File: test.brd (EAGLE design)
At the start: 28.9 x 20.9 mm, 14 parts

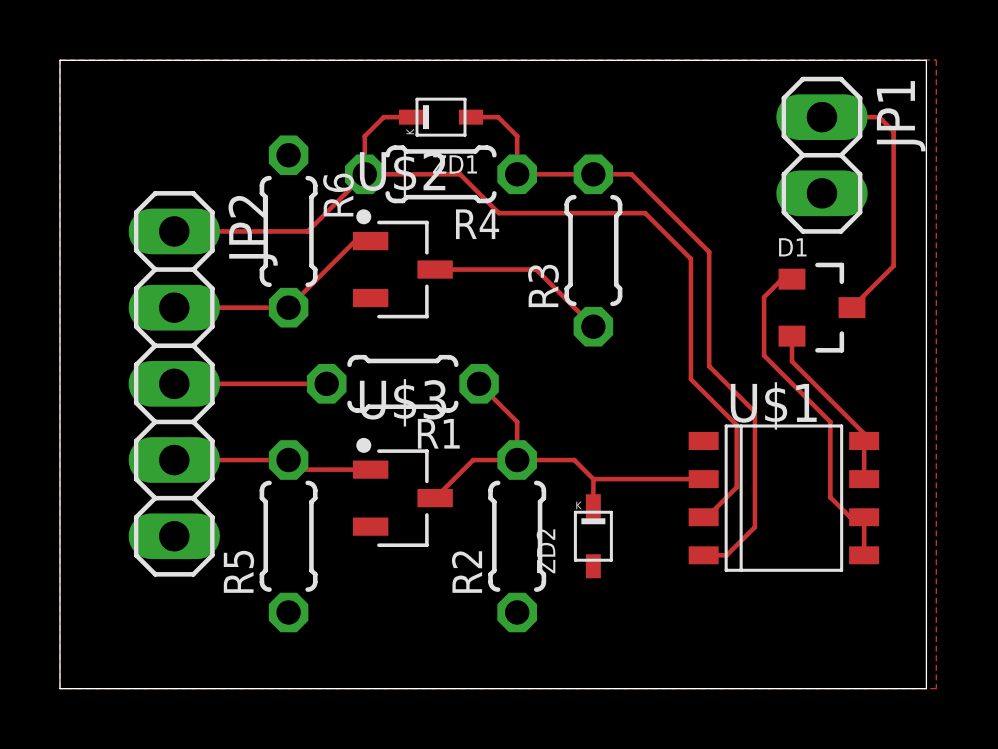
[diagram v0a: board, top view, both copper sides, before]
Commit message: added a NPN for like voltage follower
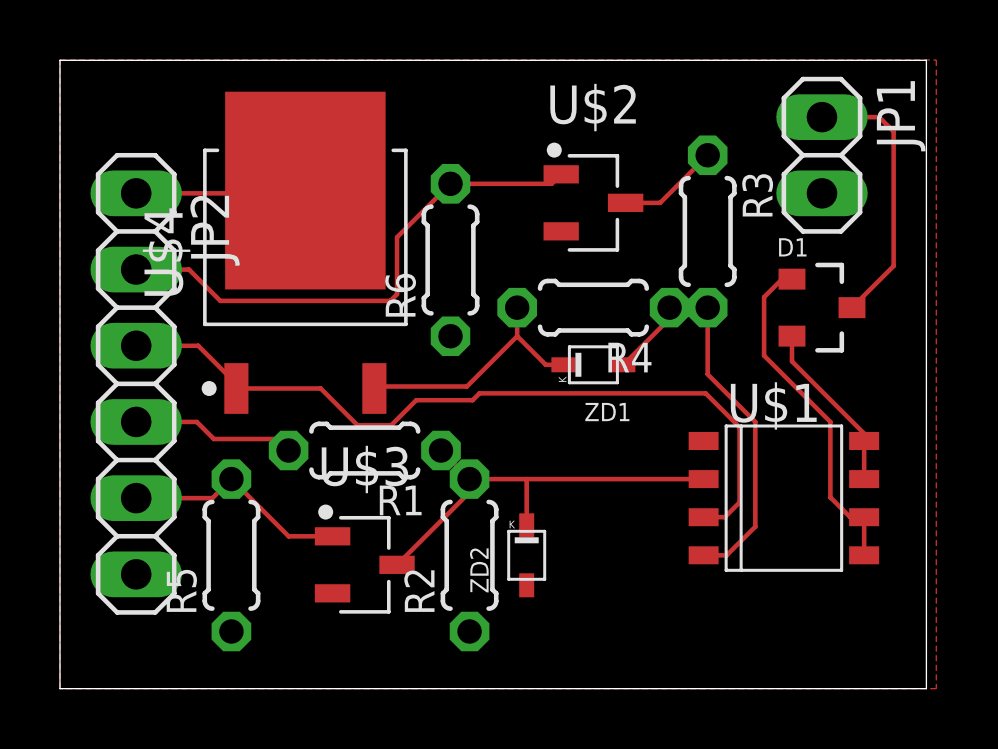
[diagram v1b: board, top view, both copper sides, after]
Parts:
- added U$4: SC3632-Z, Transistor-NPN:TO252(MP-3Z)
- JP2: device pinhead:1X05 -> pinhead:1X06
- moved ZD1 9.69 mm to (17.8, 10.8)
- moved R4 6.75 mm to (17.8, 12.7)
- moved U$2 6.73 mm to (17.8, 16.2)
- moved R6 5.48 mm to (13.0, 14.3), turned to 90 degrees
- moved R3 3.86 mm to (21.6, 15.2), turned to 270 degrees
- moved R1 2.56 mm to (10.2, 7.94)
- moved U$3 2.56 mm to (10.2, 4.13)
- moved ZD2 2.31 mm to (15.6, 4.45)
- moved R5 2.01 mm to (5.71, 4.45)
- moved R2 1.71 mm to (13.7, 4.45)
- moved JP2 1.27 mm to (2.54, 10.2)
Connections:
- new net N$6: R4.2, U$4.2, ZD1.P$1
- new net VDD: JP2.1, U$4.3
- net +12V: now also JP2.4; no longer JP2.3
- net GND: now also JP2.6; no longer JP2.5
- net N$4: now also JP2.5; no longer JP2.4
- net VPP: now also JP2.3, U$4.1; no longer JP2.1, R4.2, ZD1.P$1
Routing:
- net N$5: track 7.47 -> 17.5 mm
- net N$3: track 22.4 -> 13.9 mm
- net N$6: track 0.00 -> 8.37 mm
- net VDD: track 0.00 -> 5.68 mm
- net VPP: track 32.0 -> 26.6 mm
- net N$2: track 6.06 -> 3.39 mm
- net N$4: track 6.68 -> 7.60 mm
- net N$1: track 13.7 -> 14.5 mm

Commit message: rearranged devices
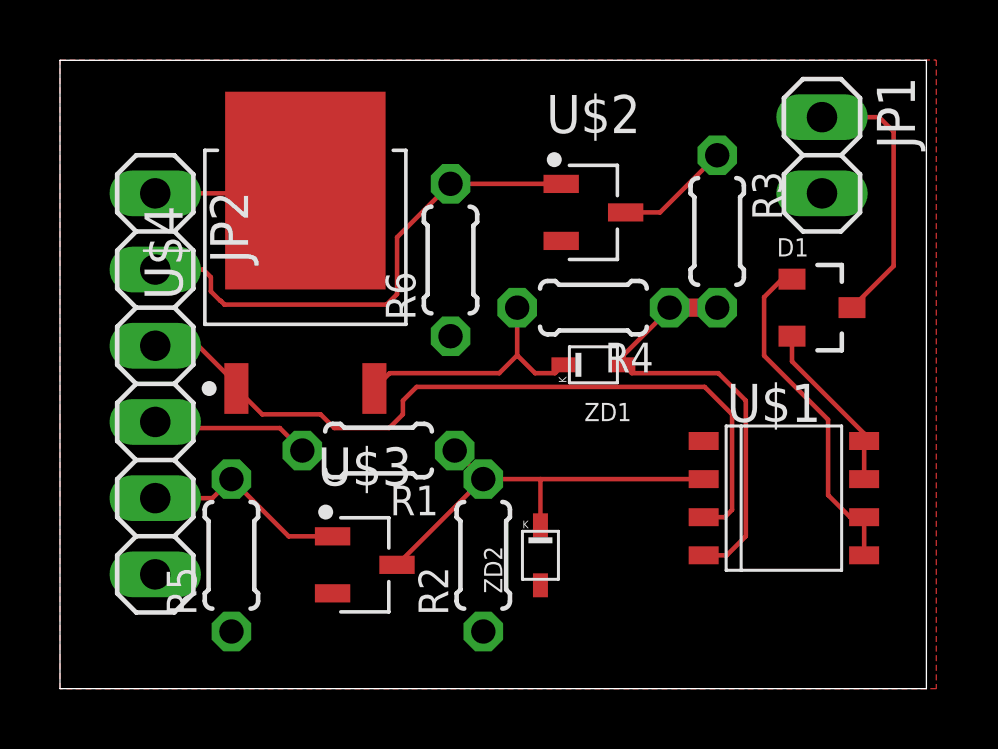
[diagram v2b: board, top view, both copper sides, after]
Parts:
- moved JP2 0.63 mm to (3.17, 10.2)
- moved ZD2 0.46 mm to (16.0, 4.45)
- moved R1 0.46 mm to (10.6, 7.94)
- moved R2 0.46 mm to (14.1, 4.45)
- moved R3 0.32 mm to (21.9, 15.2)
- moved U$2 0.32 mm to (17.8, 15.9)
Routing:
- net N$3: track 13.9 -> 14.9 mm
- net N$5: track 17.5 -> 18.2 mm
- net VPP: track 26.6 -> 25.9 mm
- net VDD: track 5.68 -> 5.04 mm
- net N$4: track 7.60 -> 6.96 mm

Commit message: replace the transistor with FET which compose a source follower.*
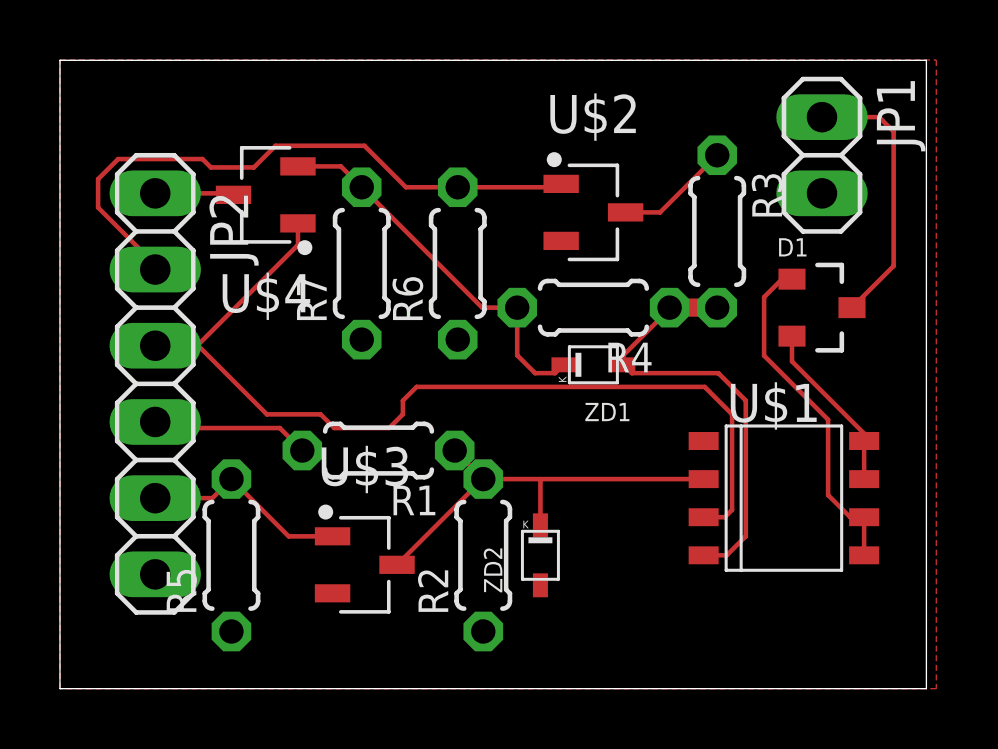
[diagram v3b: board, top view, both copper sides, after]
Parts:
- added R7: 105, rcl:0204/5
- U$4: value SC3632-Z -> 2SK3072-TB-E; device Transistor-NPN:TO252(MP-3Z) -> Transistor-FET:SOT95P250X120-3
- moved U$4 2.34 mm to (6.86, 16.5), turned to 180 degrees
- moved R6 0.27 mm to (13.3, 14.2)
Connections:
- net GND: now also R7.1
- net N$6: now also R7.2
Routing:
- net VPP: track 25.9 -> 31.3 mm
- net N$6: track 8.71 -> 12.7 mm
- net VDD: track 5.04 -> 2.63 mm
- net N$5: track 18.2 -> 20.5 mm
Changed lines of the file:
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@@
 <attribute name="VALUE" x="8.0264" y="2.3114" size="0.9906" layer="27" ratio="10" rot="R90"/>
 </element>
-<element name="R6" library="rcl" library_urn="urn:adsk.eagle:library:334" package="0204/5" package3d_urn="urn:adsk.eagle:package:23488/1" value="103" x="13.0175" y="14.2875" smashed="yes" rot="R90">
-<attribute name="NAME" x="11.8491" y="12.2809" size="0.9906" layer="25" ratio="10" rot="R90"/>
-<attribute name="SPICEPREFIX" value="R" x="49.8475" y="30.7975" size="1.778" layer="27" rot="R90" display="off"/>
-<attribute name="VALUE" x="15.3289" y="12.1539" size="0.9906" layer="27" ratio="10" rot="R90"/>
+<element name="R6" library="rcl" library_urn="urn:adsk.eagle:library:334" package="0204/5" package3d_urn="urn:adsk.eagle:package:23488/1" value="103" x="13.2588" y="14.1732" smashed="yes" rot="R90">
+<attribute name="NAME" x="12.0904" y="12.1666" size="0.9906" layer="25" ratio="10" rot="R90"/>
+<attribute name="SPICEPREFIX" value="R" x="50.0888" y="30.6832" size="1.778" layer="27" rot="R90" display="off"/>
+<attribute name="VALUE" x="15.5702" y="12.0396" size="0.9906" layer="27" ratio="10" rot="R90"/>
 </element>
 <element name="U$1" library="TC1550" library_urn="urn:adsk.eagle:library:9976041" package="SOIC-08LG" package3d_urn="urn:adsk.eagle:package:9976043/1" value="TC1550TG" x="24.13" y="6.35" smashed="yes" rot="R270">
@@
 <attribute name="VALUE" x="17.2847" y="3.175" size="0.6096" layer="27" rot="R90" align="top-left"/>
 </element>
-<element name="U$4" library="Transistor-NPN" library_urn="urn:adsk.eagle:library:11967480" package="TO252(MP-3Z)" package3d_urn="urn:adsk.eagle:package:11967296/2" value="SC3632-Z" x="8.1788" y="14.5288" smashed="yes" rot="R90">
-<attribute name="NAME" x="4.0866" y="14.5288" size="1.27" layer="25" rot="R90" align="bottom-center"/>
-<attribute name="VALUE" x="12.1638" y="14.5288" size="1.27" layer="27" rot="R90" align="top-center"/>
+<element name="U$4" library="Transistor-FET" library_urn="urn:adsk.eagle:library:11887002" package="SOT95P250X120-3" package3d_urn="urn:adsk.eagle:package:11886978/1" value="2SK3072-TB-E" x="6.858" y="16.4592" smashed="yes" rot="R180">
+<attribute name="NAME" x="6.858" y="13.8156" size="1.27" layer="25" rot="R180" align="bottom-center"/>
+<attribute name="VALUE" x="6.858" y="18.6628" size="1.27" layer="27" rot="R180" align="top-center"/>
+</element>
+<element name="R7" library="rcl" library_urn="urn:adsk.eagle:library:334" package="0204/5" package3d_urn="urn:adsk.eagle:package:23488/1" value="105" x="10.0584" y="14.1732" smashed="yes" rot="R90">
+<attribute name="NAME" x="8.89" y="12.1666" size="0.9906" layer="25" ratio="10" rot="R90"/>
+<attribute name="SPICEPREFIX" value="R" x="10.0584" y="14.1732" size="1.778" layer="27" rot="R90" display="off"/>
+<attribute name="VALUE" x="12.3698" y="12.0396" size="0.9906" layer="27" ratio="10" rot="R90"/>
 </element>
 </elements>
@@
 </polygon>
 <contactref element="JP2" pad="6"/>
+<contactref element="R7" pad="1"/>
 </signal>
 <signal name="N$2">
@@
 <contactref element="U$2" pad="1"/>
 <contactref element="JP2" pad="2"/>
-<wire x1="10.8883625" y1="12.8016" x2="11.23475" y2="13.1479875" width="0.1524" layer="1"/>
-<wire x1="11.23475" y1="13.1479875" x2="11.23475" y2="15.04475" width="0.1524" layer="1"/>
-<wire x1="11.23475" y1="15.04475" x2="13.0175" y2="16.8275" width="0.1524" layer="1"/>
-<wire x1="16.7055" y1="16.825" x2="16.703" y2="16.8275" width="0.1524" layer="1"/>
-<wire x1="13.0175" y1="16.8275" x2="16.703" y2="16.8275" width="0.1524" layer="1"/>
-<wire x1="3.175" y1="13.97" x2="4.3008375" y2="13.97" width="0.1524" layer="1"/>
-<wire x1="5.4692375" y1="12.8016" x2="5.4864" y2="12.8016" width="0.1524" layer="1"/>
-<wire x1="5.4864" y1="12.8016" x2="10.8883625" y2="12.8016" width="0.1524" layer="1"/>
-<wire x1="3.175" y1="13.97" x2="4.7752" y2="13.97" width="0.1524" layer="1"/>
-<wire x1="4.7752" y1="13.97" x2="5.0292" y2="13.716" width="0.1524" layer="1"/>
-<wire x1="5.3460375" y1="12.9248" x2="5.3632" y2="12.9248" width="0.1524" layer="1"/>
-<wire x1="5.3632" y1="12.9248" x2="5.4864" y2="12.8016" width="0.1524" layer="1"/>
-<wire x1="5.0292" y1="13.2416375" x2="5.3460375" y2="12.9248" width="0.1524" layer="1"/>
-<wire x1="5.0292" y1="13.716" x2="5.0292" y2="13.2416375" width="0.1524" layer="1"/>
+<wire x1="16.7055" y1="16.825" x2="16.5937" y2="16.7132" width="0.1524" layer="1"/>
+<wire x1="16.5937" y1="16.7132" x2="13.2588" y2="16.7132" width="0.1524" layer="1"/>
+<wire x1="11.5311625" y1="16.7132" x2="13.2588" y2="16.7132" width="0.1524" layer="1"/>
+<wire x1="1.27" y1="16.03655" x2="1.27" y2="16.98345" width="0.1524" layer="1"/>
+<wire x1="1.27" y1="16.98345" x2="1.93955" y2="17.653" width="0.1524" layer="1"/>
+<wire x1="3.175" y1="13.97" x2="3.175" y2="14.13155" width="0.1524" layer="1"/>
+<wire x1="3.175" y1="14.13155" x2="1.27" y2="16.03655" width="0.1524" layer="1"/>
+<wire x1="1.93955" y1="17.653" x2="4.7498" y2="17.653" width="0.1524" layer="1"/>
+<wire x1="4.7498" y1="17.653" x2="5.0292" y2="17.3736" width="0.1524" layer="1"/>
+<wire x1="7.1846375" y1="18.0948" x2="10.1495625" y2="18.0948" width="0.1524" layer="1"/>
+<wire x1="10.1495625" y1="18.0948" x2="11.5311625" y2="16.7132" width="0.1524" layer="1"/>
+<wire x1="5.0292" y1="17.3736" x2="6.4634375" y2="17.3736" width="0.1524" layer="1"/>
+<wire x1="6.4634375" y1="17.3736" x2="7.1846375" y2="18.0948" width="0.1524" layer="1"/>
 </signal>
 <signal name="N$7">
@@
 <signal name="VPP">
 <contactref element="U$1" pad="3"/>
-<contactref element="U$4" pad="1"/>
 <contactref element="JP2" pad="3"/>
-<wire x1="5.8788" y1="10.16" x2="5.8788" y2="10.005" width="0.1524" layer="1"/>
-<wire x1="3.175" y1="11.43" x2="4.6088" y2="11.43" width="0.1524" layer="1"/>
-<wire x1="4.6088" y1="11.43" x2="5.8788" y2="10.16" width="0.1524" layer="1"/>
-<wire x1="5.8788" y1="10.005" x2="6.7398" y2="9.144" width="0.1524" layer="1"/>
+<wire x1="3.175" y1="11.43" x2="4.572" y2="11.43" width="0.1524" layer="1"/>
+<wire x1="4.572" y1="11.43" x2="4.6088" y2="11.43" width="0.1524" layer="1"/>
 <wire x1="22.4028" y1="9.144" x2="22.4028" y2="5.9589875" width="0.1524" layer="1"/>
 <wire x1="22.4028" y1="5.9589875" x2="22.1588125" y2="5.715" width="0.1524" layer="1"/>
@@
 <wire x1="11.43" y1="9.144" x2="11.43" y2="9.6012" width="0.1524" layer="1"/>
 <wire x1="11.43" y1="9.6012" x2="11.8872" y2="10.0584" width="0.1524" layer="1"/>
-<wire x1="6.7398" y1="9.144" x2="8.6868" y2="9.144" width="0.1524" layer="1"/>
+<contactref element="U$4" pad="1"/>
+<wire x1="6.8948" y1="9.144" x2="8.6868" y2="9.144" width="0.1524" layer="1"/>
+<wire x1="4.6088" y1="11.43" x2="6.8948" y2="9.144" width="0.1524" layer="1"/>
+<wire x1="7.9325" y1="15.5092" x2="7.9325" y2="14.7905" width="0.1524" layer="1"/>
+<wire x1="7.9325" y1="14.7905" x2="4.572" y2="11.43" width="0.1524" layer="1"/>
 </signal>
 <signal name="N$4">
@@
 <contactref element="R4" pad="2"/>
 <contactref element="ZD1" pad="P$1"/>
-<contactref element="U$4" pad="2"/>
 <wire x1="16.78" y1="10.795" x2="16.5006" y2="10.5156" width="0.1524" layer="1"/>
 <wire x1="16.5006" y1="10.5156" x2="15.8369" y2="10.5156" width="0.1524" layer="1"/>
 <wire x1="15.8369" y1="10.5156" x2="15.24" y2="11.1125" width="0.1524" layer="1"/>
-<wire x1="10.4788" y1="10.005" x2="10.9894" y2="10.5156" width="0.1524" layer="1"/>
-<wire x1="10.9894" y1="10.5156" x2="14.6431" y2="10.5156" width="0.1524" layer="1"/>
-<wire x1="14.6431" y1="10.5156" x2="15.24" y2="11.1125" width="0.1524" layer="1"/>
 <wire x1="15.24" y1="11.1125" x2="15.24" y2="12.7" width="0.1524" layer="1"/>
+<contactref element="U$4" pad="2"/>
+<contactref element="R7" pad="2"/>
+<wire x1="7.9325" y1="17.4092" x2="9.3624" y2="17.4092" width="0.1524" layer="1"/>
+<wire x1="9.3624" y1="17.4092" x2="10.0584" y2="16.7132" width="0.1524" layer="1"/>
+<wire x1="10.0584" y1="16.7132" x2="14.0716" y2="12.7" width="0.1524" layer="1"/>
+<wire x1="14.0716" y1="12.7" x2="15.24" y2="12.7" width="0.1524" layer="1"/>
 </signal>
 <signal name="VDD">
+<contactref element="JP2" pad="1"/>
 <contactref element="U$4" pad="3"/>
-<contactref element="JP2" pad="1"/>
-<wire x1="3.175" y1="16.51" x2="8.0867" y2="16.51" width="0.1524" layer="1"/>
-<wire x1="8.0867" y1="16.51" x2="8.1788" y2="16.6021" width="0.1524" layer="1"/>
+<wire x1="3.175" y1="16.51" x2="5.7327" y2="16.51" width="0.1524" layer="1"/>
+<wire x1="5.7327" y1="16.51" x2="5.7835" y2="16.4592" width="0.1524" layer="1"/>
 </signal>
 </signals>

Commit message: replaced FETs for switching with cheaper lower breakdown voltage ones; and a added high voltage capacitor
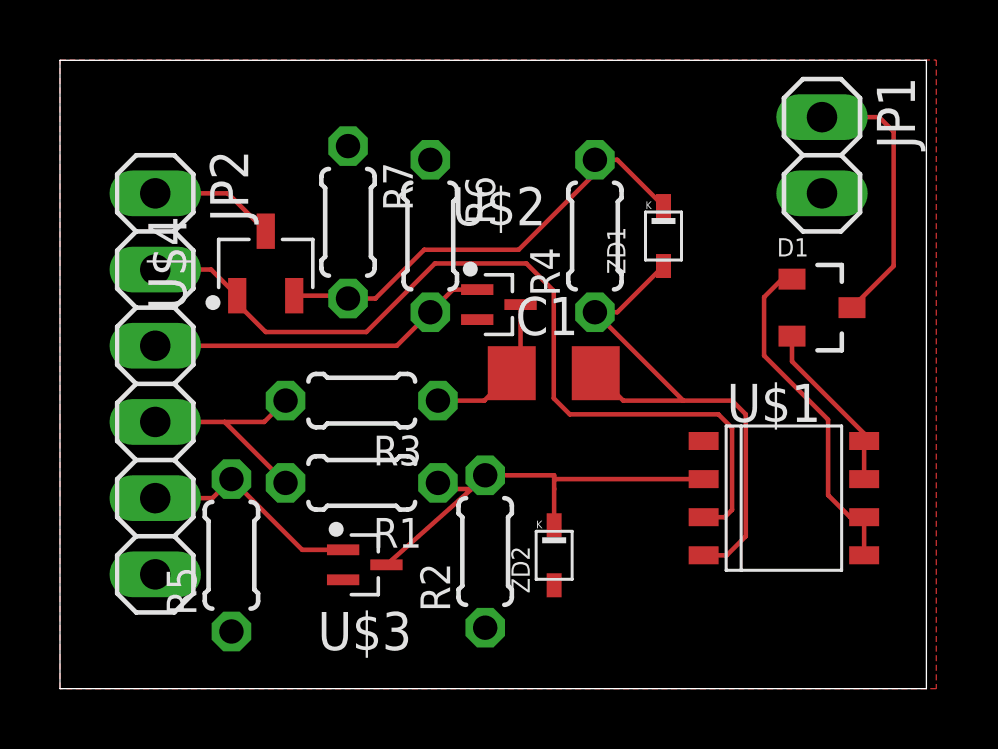
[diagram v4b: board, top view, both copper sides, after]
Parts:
- added C1: (no value), rcl:C3216
- R3: value 105 -> 103
- U$2, U$3: value 2SK3072-TB-E -> RUE002N002TL; device Transistor-FET:SOT95P250X120-3 -> Transistor-FET:SOT50P160X80-3
- moved R3 13.1 mm to (10.1, 9.60), turned to 180 degrees
- moved ZD1 4.89 mm to (20.1, 15.1), turned to 0 degrees
- moved U$2 4.40 mm to (14.6, 12.8)
- moved R4 2.39 mm to (17.8, 15.1), turned to 90 degrees
- moved U$4 2.29 mm to (6.86, 14.2), turned to 90 degrees
- moved R7 1.45 mm to (9.60, 15.5), turned to 270 degrees
- moved R6 1.29 mm to (12.3, 15.1), turned to 270 degrees
- moved R1 1.22 mm to (10.1, 6.86)
- moved ZD2 0.46 mm to (16.5, 4.45)
- moved R2 0.14 mm to (14.2, 4.57)
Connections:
- net +12V: now also R3.2
- net N$2: now also C1.1
- net N$3: now also C1.2; no longer R3.2
- net N$5: now also JP2.3; no longer JP2.2
- net VPP: now also JP2.2; no longer JP2.3
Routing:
- net N$5: track 20.5 -> 11.5 mm
- net N$3: track 14.9 -> 18.4 mm
- net +12V: track 5.30 -> 8.44 mm
- net N$6: track 12.7 -> 15.2 mm
- net VPP: track 31.3 -> 29.3 mm
- net VDD: track 2.63 -> 4.21 mm
- net N$2: track 3.84 -> 5.11 mm
- net N$4: track 6.96 -> 7.50 mm

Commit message: replace lower voltage FET by CMOS for putting off a CR circuit between HiVol-PMOS-Gate and 12V source.
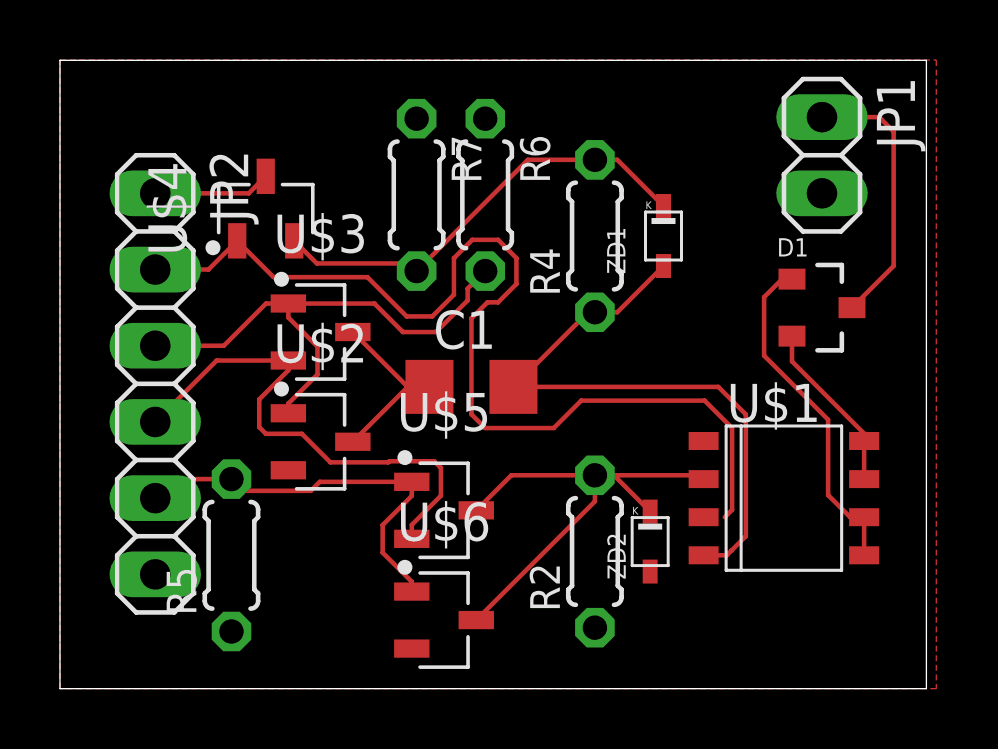
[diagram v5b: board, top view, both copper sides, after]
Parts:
- removed R1, R3: 103, rcl:0204/5
- added U$5: IRLML2246TRPBFTR, Transistor-FET:SOT95P250X120-3
- added U$6: IRLML6344TRPBFTR, Transistor-FET:SOT95P250X120-3
- U$2: value RUE002N002TL -> IRLML6344TRPBFTR; device Transistor-FET:SOT50P160X80-3 -> Transistor-FET:SOT95P250X120-3
- U$3: value RUE002N002TL -> IRLML2246TRPBFTR; device Transistor-FET:SOT50P160X80-3 -> Transistor-FET:SOT95P250X120-3
- moved U$3 7.90 mm to (8.69, 11.9)
- moved U$2 7.50 mm to (8.69, 8.23)
- moved R2 3.66 mm to (17.8, 4.57)
- moved ZD2 3.23 mm to (19.7, 4.90)
- moved C1 2.78 mm to (13.7, 10.1)
- moved R7 2.46 mm to (11.9, 16.5)
- moved R6 2.29 mm to (14.2, 16.5)
- moved U$4 1.83 mm to (6.86, 16.0)
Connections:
- net +12V: now also U$3.2, U$5.2; no longer R1.2, R3.2
- net GND: now also U$6.2; no longer U$3.2
- net N$1: now also U$5.3, U$6.3; no longer R1.1, U$3.3
- net N$2: now also U$3.3; no longer R3.1
- net N$4: now also U$5.1, U$6.1; no longer U$3.1
- net N$5: now also U$3.1
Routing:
- net +12V: track 8.44 -> 17.5 mm
- net N$4: track 7.50 -> 13.6 mm
- net N$5: track 11.5 -> 17.5 mm
- net VPP: track 29.3 -> 34.2 mm
- net N$1: track 14.7 -> 16.9 mm
- net N$3: track 18.4 -> 20.5 mm
- net N$2: track 5.11 -> 5.90 mm
